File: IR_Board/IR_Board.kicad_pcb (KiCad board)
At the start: 2 copper layers, 189.9 x 157.6 mm, 64 parts, among them J1 Conn_02x08_Top_Bottom, Q1 FDG6335N, Q10 FDG6335N, Q11 FDG6335N, Q12 FDG6335N, Q13 FDG6335N, Q14 FDG6335N, Q2 FDG6335N, Q3 FDG6335N, Q4 FDG6335N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

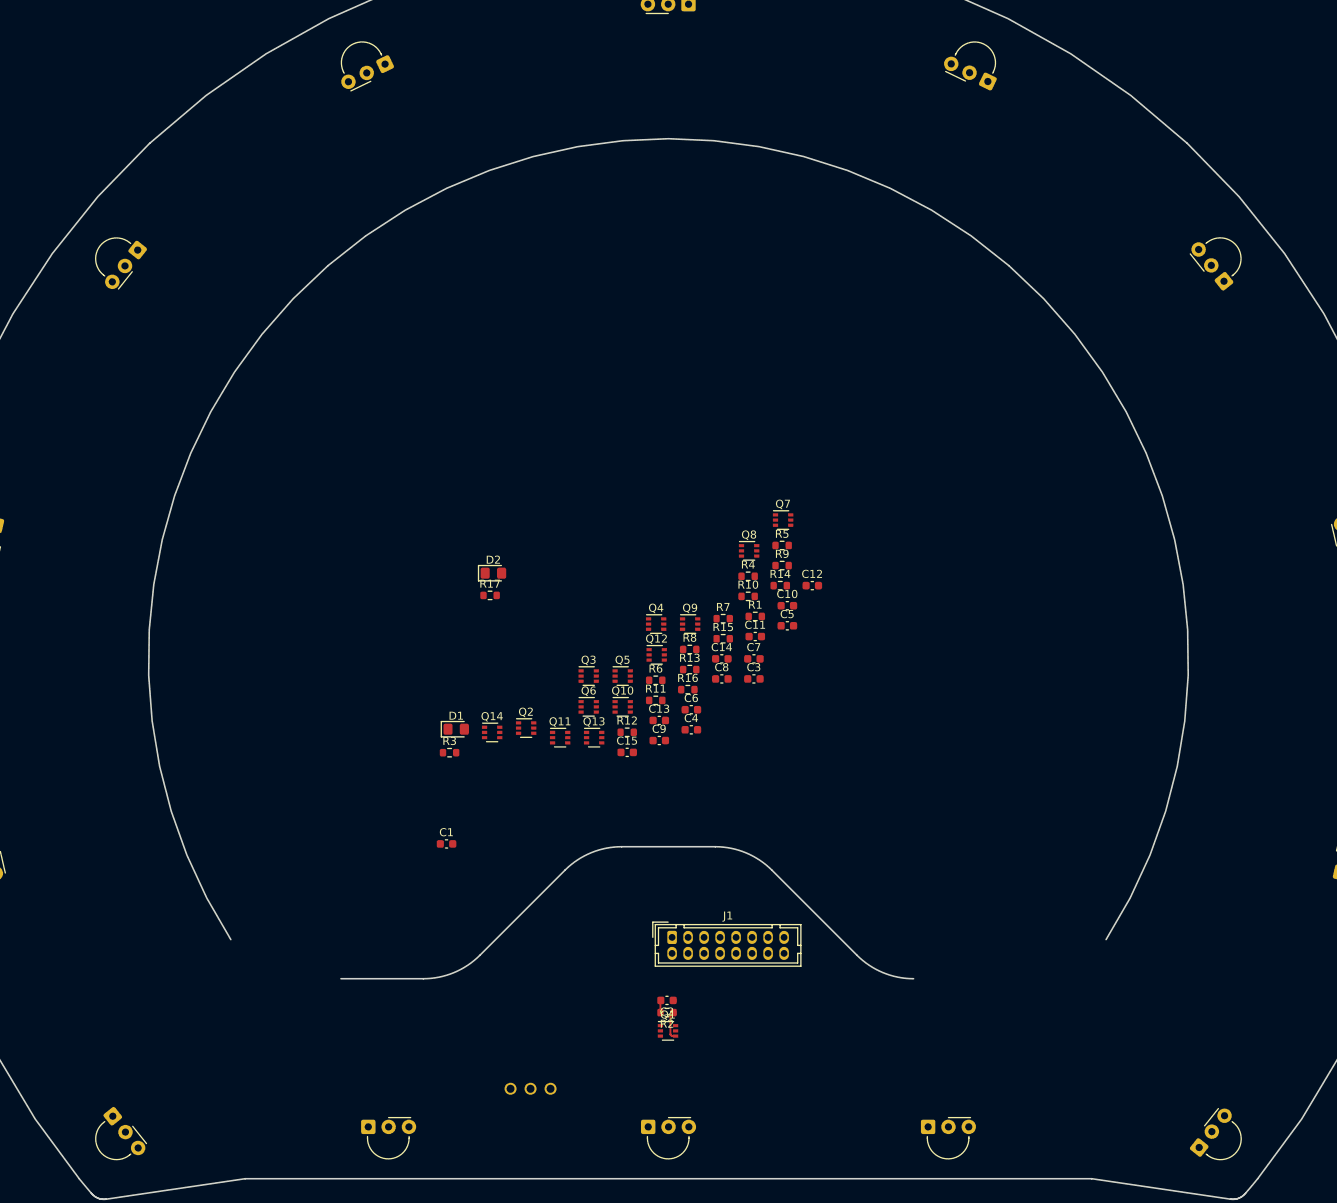
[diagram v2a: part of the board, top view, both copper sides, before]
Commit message: Progress with pcb [IR BOARD]
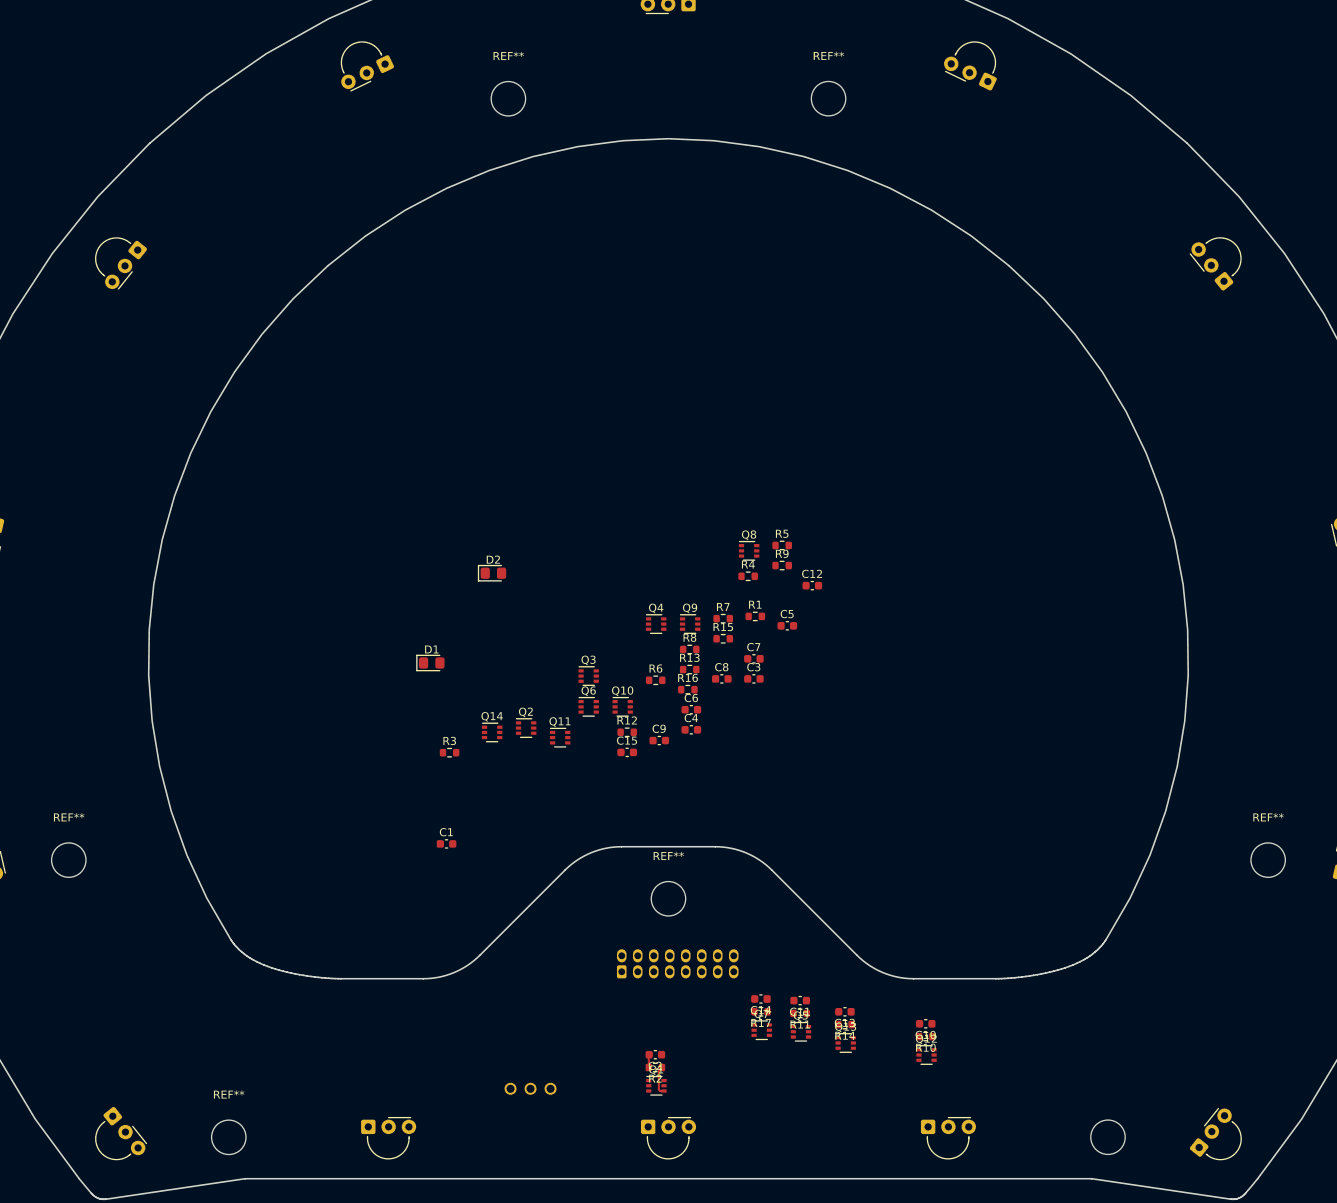
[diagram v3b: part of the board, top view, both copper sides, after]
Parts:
- added REF**: MountingHole_4.3mm_M4, MountingHole:MountingHole_4.3mm_M4, F.Cu at (226.4, 130.0)
- added REF**: MountingHole_4.3mm_M4, MountingHole:MountingHole_4.3mm_M4, F.Cu at (131.4, 34.9)
- added REF**: MountingHole_4.3mm_M4, MountingHole:MountingHole_4.3mm_M4, F.Cu at (151.4, 134.9)
- added REF**: MountingHole_4.3mm_M4, MountingHole:MountingHole_4.3mm_M4, F.Cu at (76.5, 130.0)
- added REF**: MountingHole_4.3mm_M4, MountingHole:MountingHole_4.3mm_M4, F.Cu at (96.5, 164.7)
- added REF**: MountingHole_4.3mm_M4, MountingHole:MountingHole_4.3mm_M4, F.Cu at (171.4, 34.9)
- added REF**: MountingHole_4.3mm_M4, MountingHole:MountingHole_4.3mm_M4, B.Cu at (206.4, 164.7)
- J1: moved to B.Cu
- moved Q7 63.8 mm to (163.1, 151.3)
- moved R17 62.1 mm to (163.0, 149.0), turned to 180 degrees
- moved Q12 60.3 mm to (183.7, 154.4)
- moved R10 59.3 mm to (183.6, 152.1), turned to 180 degrees
- moved R14 55.5 mm to (173.5, 150.6), turned to 180 degrees
- moved C10 55.0 mm to (183.6, 150.5), turned to 180 degrees
- moved Q5 49.7 mm to (168.0, 151.5)
- moved Q13 49.5 mm to (173.6, 152.9)
- moved C11 45.9 mm to (167.9, 147.6), turned to 180 degrees
- moved C13 43.2 mm to (173.5, 149.0), turned to 180 degrees
- moved R11 43.1 mm to (167.9, 149.2), turned to 180 degrees
- moved C14 42.8 mm to (163.0, 147.4), turned to 180 degrees
- moved D1 8.82 mm to (121.8, 105.4)
- moved J1 7.62 mm to (145.6, 144.0)
- moved Q1 7.02 mm to (149.9, 158.2)
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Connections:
- C1 pad 1: +3V3 -> GND
- C1 pad 2: GND -> +3V3
- C10 pad 2: Net-(C10-Pad2) -> IR12
- C11 pad 2: Net-(C11-Pad2) -> IR5
- C12 pad 2: Net-(C12-Pad2) -> IR6
- C13 pad 2: Net-(C13-Pad2) -> IR13
- C14 pad 2: Net-(C14-Pad2) -> IR7
- C15 pad 2: Net-(C15-Pad2) -> IR14
- C2 pad 2: Net-(C2-Pad2) -> IR1
- C3 pad 2: Net-(C3-Pad2) -> IR8
- C4 pad 2: Net-(C4-Pad2) -> IR2
- C5 pad 2: Net-(C5-Pad2) -> IR9
- C6 pad 2: Net-(C6-Pad2) -> IR3
- C7 pad 2: Net-(C7-Pad2) -> IR10
- C8 pad 2: Net-(C8-Pad2) -> IR4
- C9 pad 2: Net-(C9-Pad2) -> IR11
- J1 pad 1: GND -> IR1
- J1 pad 10: Net-(C3-Pad2) -> IR10
- J1 pad 11: Net-(C5-Pad2) -> IR11
- J1 pad 12: Net-(C7-Pad2) -> IR12
- J1 pad 13: Net-(C9-Pad2) -> IR13
- J1 pad 14: Net-(C10-Pad2) -> IR14
- J1 pad 15: Net-(C13-Pad2) -> +3V3
- J1 pad 16: Net-(C15-Pad2) -> GND
- J1 pad 2: Net-(C2-Pad2) -> IR2
- J1 pad 3: Net-(C4-Pad2) -> IR3
- J1 pad 4: Net-(C6-Pad2) -> IR4
- J1 pad 5: Net-(C8-Pad2) -> IR5
- J1 pad 6: Net-(C11-Pad2) -> IR6
- J1 pad 7: Net-(C12-Pad2) -> IR7
- J1 pad 8: Net-(C14-Pad2) -> IR8
- J1 pad 9: +3V3 -> IR9
- Q1 pad 1: Net-(C2-Pad2) -> IR1
- Q10 pad 1: Net-(C7-Pad2) -> IR10
- Q11 pad 1: Net-(C9-Pad2) -> IR11
- Q12 pad 1: Net-(C10-Pad2) -> IR12
- Q13 pad 1: Net-(C13-Pad2) -> IR13
- Q14 pad 1: Net-(C15-Pad2) -> IR14
- Q2 pad 1: Net-(C4-Pad2) -> IR2
- Q3 pad 1: Net-(C6-Pad2) -> IR3
- Q4 pad 1: Net-(C8-Pad2) -> IR4
- Q5 pad 1: Net-(C11-Pad2) -> IR5
- Q6 pad 1: Net-(C12-Pad2) -> IR6
- Q7 pad 1: Net-(C14-Pad2) -> IR7
- Q8 pad 1: Net-(C3-Pad2) -> IR8
- Q9 pad 1: Net-(C5-Pad2) -> IR9
- R1 pad 2: Net-(C3-Pad2) -> IR8
- R10 pad 2: Net-(C10-Pad2) -> IR12
- R11 pad 2: Net-(C11-Pad2) -> IR5
- R14 pad 2: Net-(C13-Pad2) -> IR13
- R15 pad 2: Net-(C12-Pad2) -> IR6
- R16 pad 2: Net-(C15-Pad2) -> IR14
- R17 pad 2: Net-(C14-Pad2) -> IR7
- R2 pad 2: Net-(C2-Pad2) -> IR1
- R3 pad 2: Net-(C5-Pad2) -> IR9
- R4 pad 2: Net-(C4-Pad2) -> IR2
- R5 pad 2: Net-(C7-Pad2) -> IR10
- R6 pad 2: Net-(C6-Pad2) -> IR3
- R7 pad 2: Net-(C9-Pad2) -> IR11
- R8 pad 2: Net-(C8-Pad2) -> IR4
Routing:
- net Net-(C2-Pad2): track 1.54 -> 0.00 mm
- net IR1: track 0.00 -> 1.54 mm
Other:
- outline, holes or cut-outs redrawn

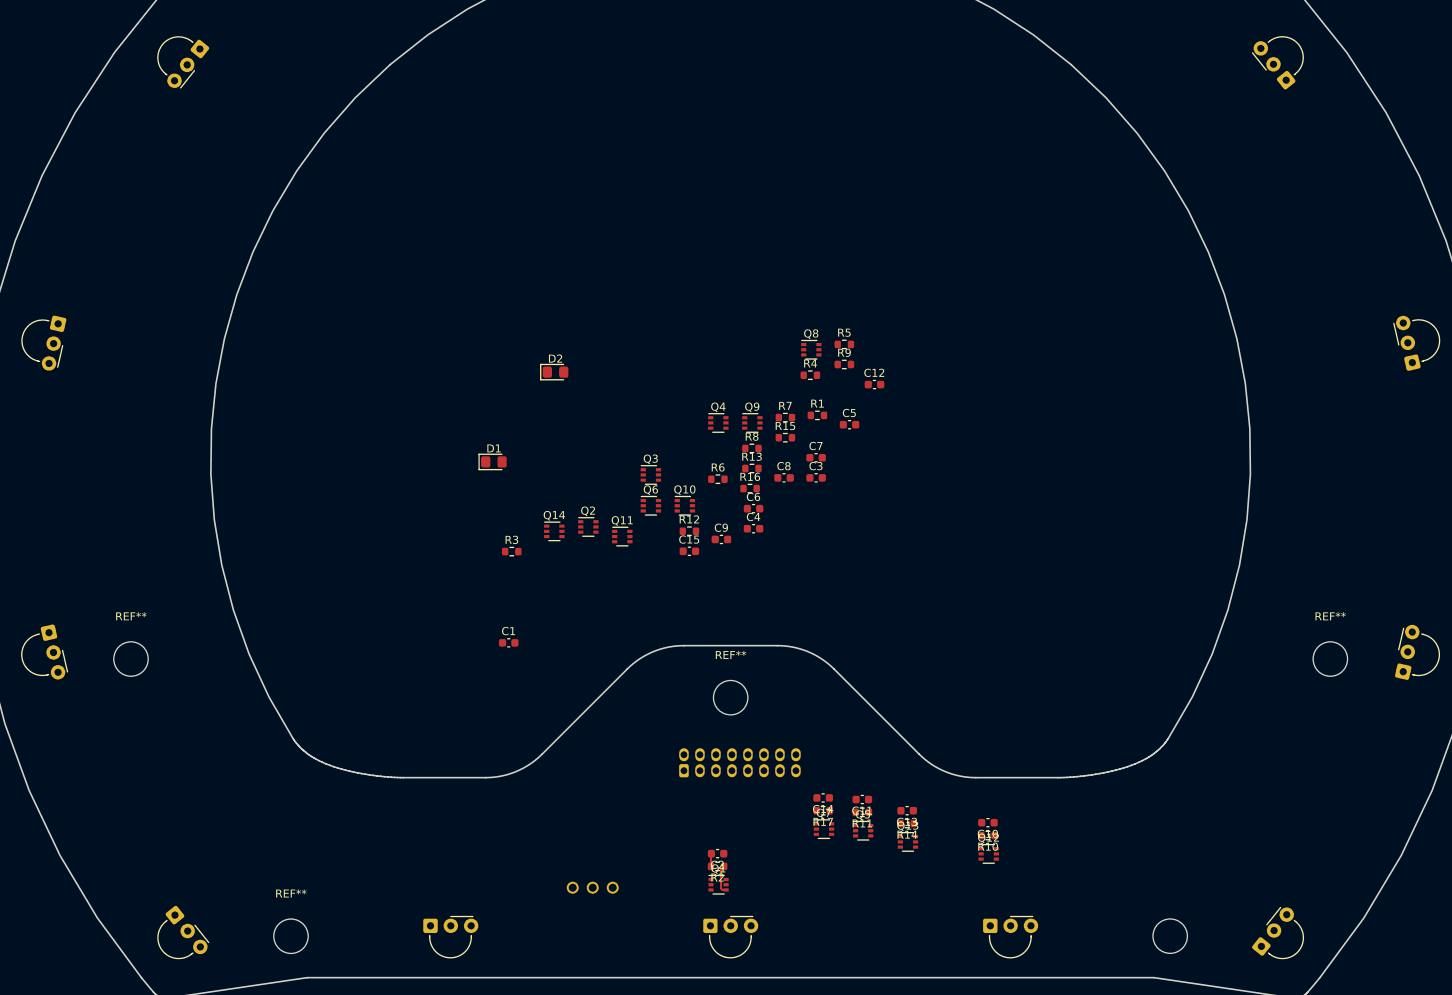
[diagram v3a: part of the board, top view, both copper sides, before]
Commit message: Started drawing traces [IR BOARD]
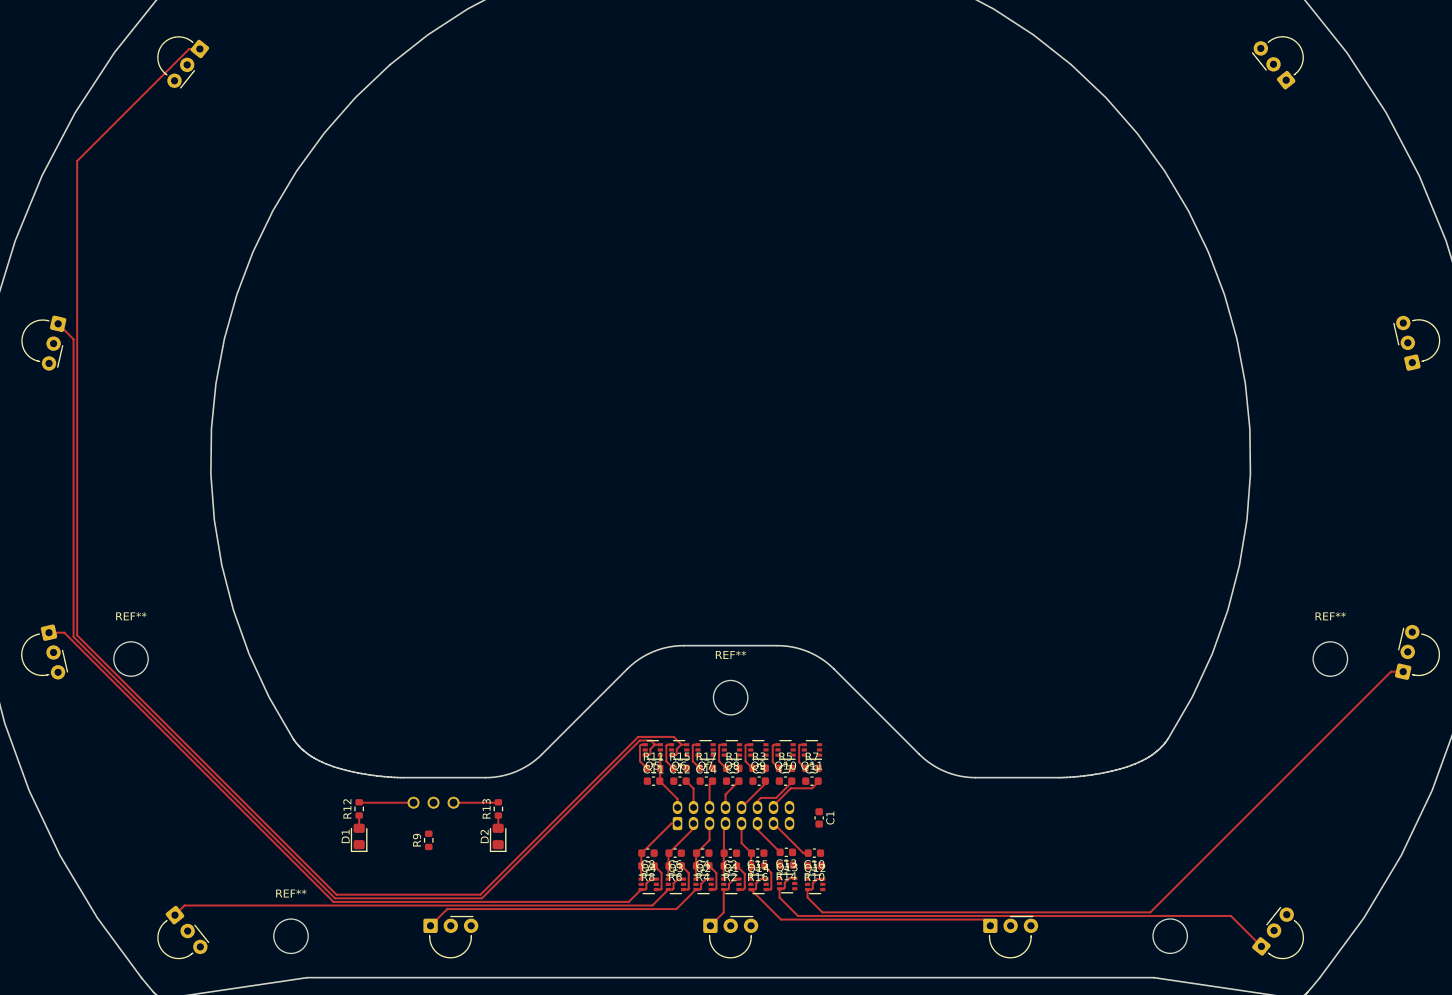
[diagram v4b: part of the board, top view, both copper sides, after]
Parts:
- moved R9 79.0 mm to (113.7, 152.7), turned to 90 degrees
- moved R4 62.8 mm to (147.9, 155.9), turned to 180 degrees
- moved D2 58.5 mm to (122.4, 152.2), turned to 90 degrees
- moved Q4 58.3 mm to (141.2, 158.2)
- moved C12 55.2 mm to (145.1, 145.3)
- moved R12 53.9 mm to (105.0, 148.8), turned to 90 degrees
- moved R8 53.8 mm to (141.1, 155.9), turned to 180 degrees
- moved R5 53.5 mm to (158.3, 143.7)
- moved R13 53.1 mm to (122.4, 148.8), turned to 90 degrees
- moved Q3 51.3 mm to (144.6, 158.2)
- moved Q8 51.0 mm to (151.6, 141.4), turned to 180 degrees
- moved Q14 51.0 mm to (154.9, 158.2)
- moved C8 49.9 mm to (141.1, 154.3), turned to 180 degrees
- moved D1 49.8 mm to (105.0, 152.2), turned to 90 degrees
- moved R6 48.6 mm to (144.5, 155.9), turned to 180 degrees
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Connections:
- J1 pad 1: IR1 -> IR4
- J1 pad 10: IR10 -> IR9
- J1 pad 11: IR11 -> IR13
- J1 pad 12: IR12 -> IR10
- J1 pad 13: IR13 -> IR12
- J1 pad 14: IR14 -> IR11
- J1 pad 2: IR2 -> IR5
- J1 pad 4: IR4 -> IR6
- J1 pad 5: IR5 -> IR2
- J1 pad 6: IR6 -> IR7
- J1 pad 7: IR7 -> IR1
- J1 pad 9: IR9 -> IR14
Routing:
- net Net-(Q6-Pad3): track 0.00 -> 180.8 mm
- net Net-(Q5-Pad3): track 0.00 -> 137.4 mm
- net Net-(Q12-Pad3): track 0.00 -> 91.5 mm
- net Net-(Q4-Pad3): track 0.00 -> 91.4 mm
- net Net-(Q13-Pad3): track 0.00 -> 66.7 mm
- net Net-(Q3-Pad3): track 0.00 -> 65.8 mm
- net Net-(Q2-Pad3): track 0.00 -> 37.8 mm
- net Net-(Q14-Pad3): track 0.00 -> 34.6 mm
- net IR4: track 0.00 -> 9.29 mm
- net IR3: track 0.00 -> 8.25 mm
- net Net-(Q1-Pad3): track 0.00 -> 7.99 mm
- net IR2: track 0.00 -> 7.65 mm
- net IR5: track 0.00 -> 7.50 mm
- net IR14: track 0.00 -> 7.50 mm
- net IR11: track 0.00 -> 7.23 mm
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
